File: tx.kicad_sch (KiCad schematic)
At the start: 44 parts, among them J5 SWH, J7 SMA, T2 RF_BALUN, U12 MAX2831, U13 TXIF_BALUN, U16 DPDT

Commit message: Add footprints
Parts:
- C86: footprint (none) -> Capacitor_SMD:C_0201_0603Metric
- FL2: footprint (none) -> mainboard:Filter_Pulse_LPF1005LL50R2400A_1.5x0.5mm
- J5: footprint (none) -> mainboard:Murata_SWH_MM8930-26xx
- J7: footprint (none) -> mainboard:Linx_SMA_CONSMA003.062
- L2, L6, L7: footprint (none) -> Inductor_SMD:L_0201_0603Metric
- T2: footprint (none) -> RF_Converter:Anaren_0805_2012Metric-6
- U13: footprint (none) -> mainboard:Balun_TDK_TFSZ06052460-3310A2X
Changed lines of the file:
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@@
       (effects (font (size 1.27 1.27)) (justify left))
     )
-    (property "Footprint" "" (at 111.76 80.01 0)
+    (property "Footprint" "Inductor_SMD:L_0201_0603Metric" (at 111.76 80.01 0)
       (effects (font (size 1.27 1.27)) hide)
     )
@@
       (effects (font (size 1.27 1.27)))
     )
-    (property "Footprint" "" (at 166.37 119.38 0)
+    (property "Footprint" "RF_Converter:Anaren_0805_2012Metric-6" (at 166.37 119.38 0)
       (effects (font (size 1.27 1.27)) hide)
     )
@@
       (effects (font (size 1.27 1.27)))
     )
-    (property "Footprint" "" (at 196.85 86.36 0)
+    (property "Footprint" "mainboard:Murata_SWH_MM8930-26xx" (at 196.85 86.36 0)
       (effects (font (size 1.27 1.27)) hide)
     )
@@
       (effects (font (size 1.27 1.27)) (justify left))
     )
-    (property "Footprint" "" (at 111.4552 148.59 0)
+    (property "Footprint" "Capacitor_SMD:C_0201_0603Metric" (at 111.4552 148.59 0)
       (effects (font (size 1.27 1.27)) hide)
     )
@@
       (effects (font (size 1.27 1.27)))
     )
-    (property "Footprint" "" (at 129.54 74.93 0)
+    (property "Footprint" "mainboard:Murata_SWH_MM8930-26xx" (at 129.54 74.93 0)
       (effects (font (size 1.27 1.27)) hide)
     )
@@
       (effects (font (size 1.27 1.27)) (justify left))
     )
-    (property "Footprint" "" (at 175.26 110.49 0)
+    (property "Footprint" "Inductor_SMD:L_0201_0603Metric" (at 175.26 110.49 0)
       (effects (font (size 1.27 1.27)) hide)
     )
@@
       (effects (font (size 1.27 1.27)) (justify left))
     )
-    (property "Footprint" "" (at 260.35 74.93 0)
+    (property "Footprint" "mainboard:Linx_SMA_CONSMA003.062" (at 260.35 74.93 0)
       (effects (font (size 1.27 1.27)) hide)
     )
@@
       (effects (font (size 1.27 1.27)))
     )
-    (property "Footprint" "" (at 146.05 62.23 0)
+    (property "Footprint" "mainboard:Filter_Pulse_LPF1005LL50R2400A_1.5x0.5mm" (at 146.05 62.23 0)
       (effects (font (size 1.27 1.27)) hide)
     )
@@
       (effects (font (size 1.27 1.27)))
     )
-    (property "Footprint" "" (at 242.57 120.65 0)
+    (property "Footprint" "mainboard:Balun_TDK_TFSZ06052460-3310A2X" (at 242.57 120.65 0)
       (effects (font (size 1.27 1.27)) hide)
     )
@@
     )
     (property "Part Number" "TFSZ06052460-3310A2X" (at 242.57 113.03 0)
+      (effects (font (size 1.27 1.27)) hide)
+    )
+    (property "Description" "BALUN 2300-2690 MHZ" (at 242.57 113.03 0)
       (effects (font (size 1.27 1.27)) hide)
     )
@@
       (effects (font (size 1.27 1.27)))
     )
-    (property "Footprint" "" (at 118.11 87.63 0)
+    (property "Footprint" "mainboard:Balun_TDK_TFSZ06052460-3310A2X" (at 118.11 87.63 0)
       (effects (font (size 1.27 1.27)) hide)
     )
@@
     )
     (property "Part Number" "TFSZ06052460-3310A2X" (at 118.11 80.01 0)
+      (effects (font (size 1.27 1.27)) hide)
+    )
+    (property "Description" "BALUN 2300-2690 MHZ" (at 118.11 80.01 0)
       (effects (font (size 1.27 1.27)) hide)
     )
@@
       (effects (font (size 1.27 1.27)) (justify left))
     )
-    (property "Footprint" "" (at 236.22 113.03 0)
-      (effects (font (size 1.27 1.27)) hide)
-    )
+    (property "Footprint" "Inductor_SMD:L_0201_0603Metric" (at 236.22 113.03 0)
+      (effects (font (size 1.27 1.27)) hide)
+    )

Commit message: Add more footprints
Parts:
- U16: footprint eval:QFN-12-1EP_2x2mm_P0.5mm_EP1x1mm -> mainboard:QFN-12-1EP_2x2mm_P0.5mm_EP1x1mm
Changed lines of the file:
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@@
       (effects (font (size 1.27 1.27)) (justify left))
     )
-    (property "Footprint" "eval:QFN-12-1EP_2x2mm_P0.5mm_EP1x1mm" (at 168.91 74.93 0)
+    (property "Footprint" "mainboard:QFN-12-1EP_2x2mm_P0.5mm_EP1x1mm" (at 168.91 74.93 0)
       (effects (font (size 1.27 1.27)) hide)
     )

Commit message: layout wip
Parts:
- added C10 (x2): 1uF, Capacitor_SMD:C_0201_0603Metric, symbol Device:C
- added J13: RFShield_Frame, RF_Shielding:Laird_Technologies_BMI-S-204-F_32.00x32.00mm, symbol Device:RFShield_OnePiece
- C36: footprint Capacitor_SMD:C_0402_1005Metric -> Capacitor_SMD:C_0201_0603Metric; Manufacturer Samsung -> Murata; Part Number CL05A105KP5NNNC -> GRM033R61A105ME44D; Substitution any equivalent -> GRM033R61A105ME44*, GRM033R61C105ME15*, Samsung CL03A105MO3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
- U16: footprint mainboard:QFN-12-1EP_2x2mm_P0.5mm_EP1x1mm -> mainboard:QFN-12-1EP_2x2mm_P0.5mm_EP1x1mm_ThermalVias
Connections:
- net 3V3TX: now also C10.1, C10.1
- net GND: now also C10.2, C10.2, J13.1 (Shield)
- net TX Mixer/MIX_IN+: now also L7.2, U13.4; no longer L7.1, U13.3
- net TX Mixer/MIX_IN-: now also L7.1, U13.3; no longer L7.2, U13.4

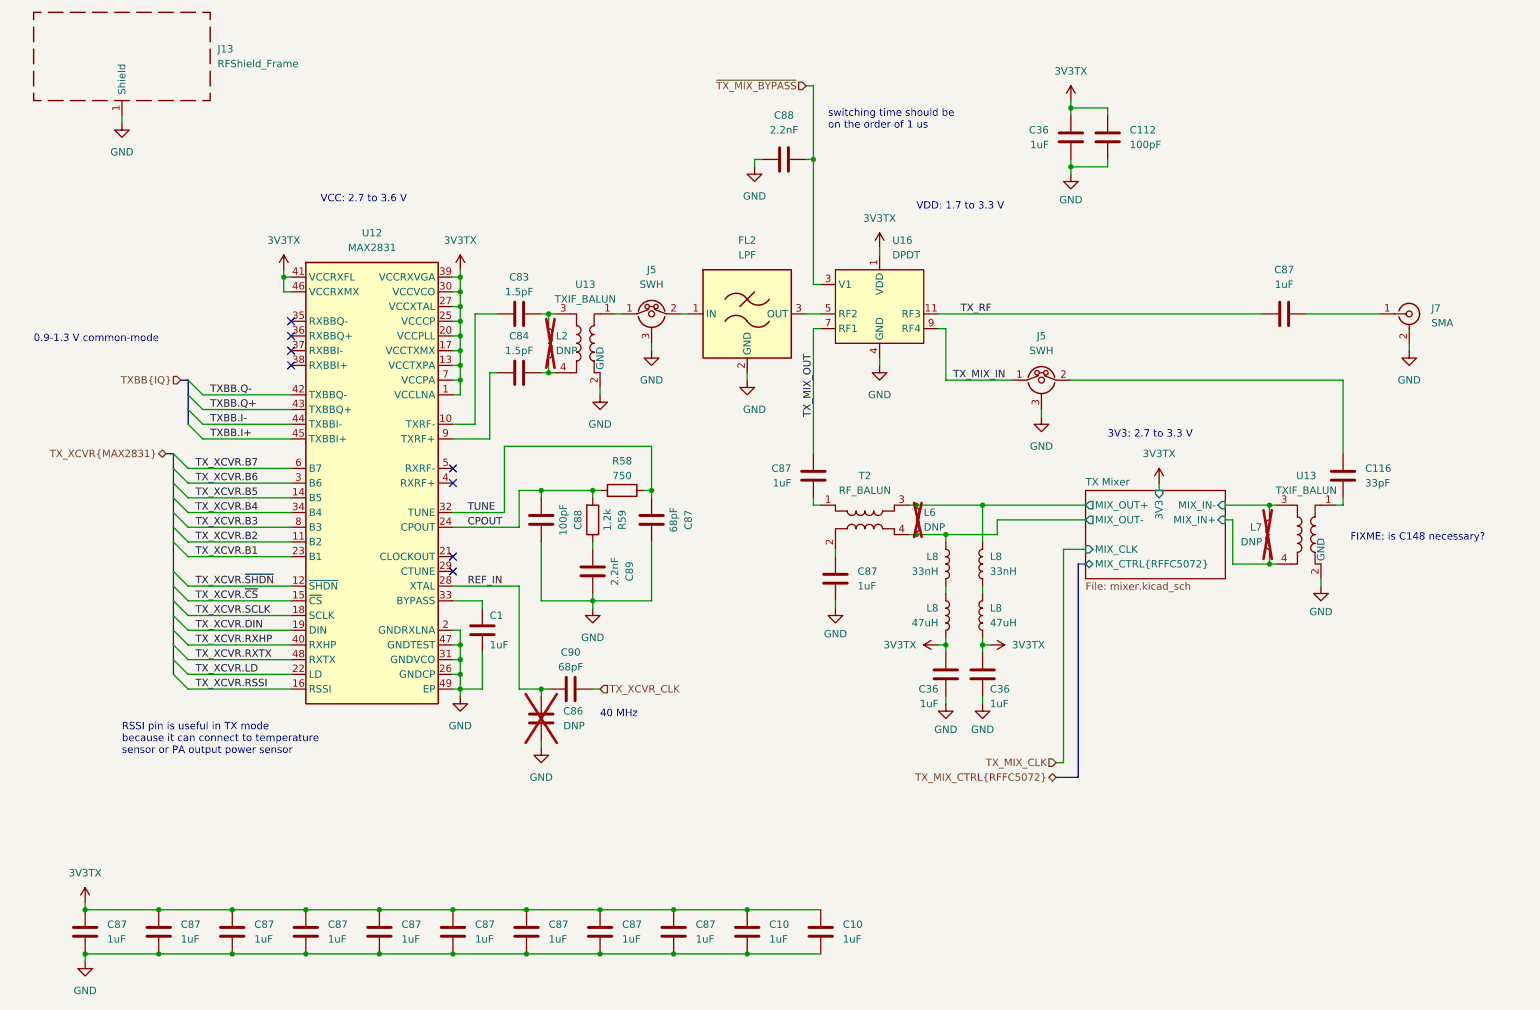
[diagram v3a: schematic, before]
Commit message: complete initial layout
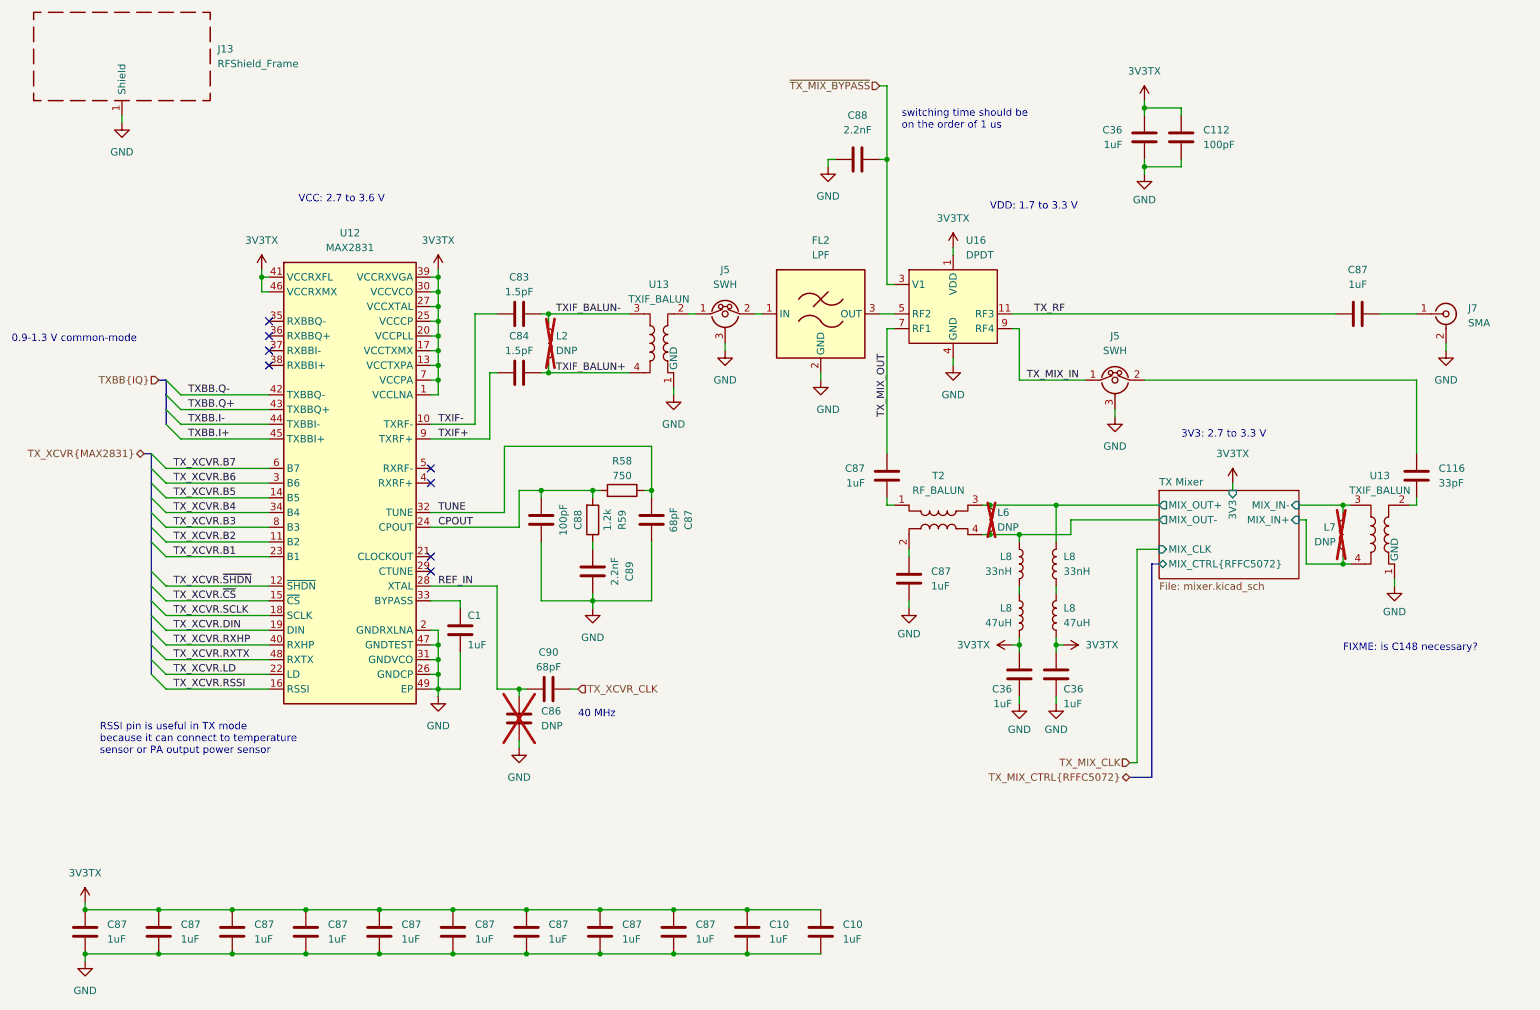
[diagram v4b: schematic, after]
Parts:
- U13: symbol Transformer:0896BM15A0001 -> radio:TFSZ06052460-3310A2X
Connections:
- net GND: now also U13.1 (GND), U13.1 (GND); no longer U13.2 (GND), U13.2 (GND), U13.5 (GND), U13.5 (GND), U13.6 (GND), U13.6 (GND)
- net TXIF_BALUN-: now reaches C83.2, L2.1, U13.3
- net TXIF_BALUN+: now reaches C84.2, L2.2, U13.4
- net TXIF-: now reaches C83.1, U12.10 (TXRF-)
- net at C116.2: now also U13.2; no longer U13.1
- net at J5.1 (C): now also U13.2; no longer U13.1
- net TXIF+: now reaches C84.1, U12.9 (TXRF+)
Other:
- moved on the sheet: C1, C112, C116, C36, C86, C87, C88, C90, FL2, J5, J7, L6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

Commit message: passive component selections
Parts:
- C83, C84: Manufacturer (none) -> Murata; Part Number (none) -> GRM0335C1H1R5CA01D; Substitution (none) -> GRM0335C1H1R5CA01*
- C87, C90: Manufacturer (none) -> Murata; Part Number (none) -> GRM0335C1H680JA01D; Substitution (none) -> GRM0335C1H680JA01*
- R58: Manufacturer (none) -> Yageo; Part Number (none) -> RC0201JR-07750RL; Substitution (none) -> any equivalent
- R59: Manufacturer (none) -> Yageo; Part Number (none) -> RC0201JR-071K2L; Substitution (none) -> any equivalent
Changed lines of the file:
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@@
+      (effects (font (size 1.27 1.27)) hide)
+    )
+    (property "Description" "RES 750 OHM 5% 1/20W 0201" (at 124.46 105.41 0)
+      (effects (font (size 1.27 1.27)) hide)
+    )
+    (property "Manufacturer" "Yageo" (at 124.46 105.41 0)
+      (effects (font (size 1.27 1.27)) hide)
+    )
+    (property "Part Number" "RC0201JR-07750RL" (at 124.46 105.41 0)
+      (effects (font (size 1.27 1.27)) hide)
+    )
+    (property "Substitution" "any equivalent" (at 124.46 105.41 0)
       (effects (font (size 1.27 1.27)) hide)
     )
@@
       (effects (font (size 1.27 1.27)) hide)
     )
+    (property "Description" "CAP CER 1.5PF 50V C0G/NP0 0201" (at 106.68 74.93 0)
+      (effects (font (size 1.27 1.27)) hide)
+    )
+    (property "Manufacturer" "Murata" (at 106.68 74.93 0)
+      (effects (font (size 1.27 1.27)) hide)
+    )
+    (property "Part Number" "GRM0335C1H1R5CA01D" (at 106.68 74.93 0)
+      (effects (font (size 1.27 1.27)) hide)
+    )
+    (property "Substitution" "GRM0335C1H1R5CA01*" (at 106.68 74.93 0)
+      (effects (font (size 1.27 1.27)) hide)
+    )
     (pin "1")
     (pin "2")
@@
       (effects (font (size 1.27 1.27)) hide)
     )
+    (property "Description" "CAP CER 68PF 50V C0G/NP0 0201" (at 111.76 139.7 0)
+      (effects (font (size 1.27 1.27)) hide)
+    )
+    (property "Manufacturer" "Murata" (at 111.76 139.7 0)
+      (effects (font (size 1.27 1.27)) hide)
+    )
+    (property "Part Number" "GRM0335C1H680JA01D" (at 111.76 139.7 0)
+      (effects (font (size 1.27 1.27)) hide)
+    )
+    (property "Substitution" "GRM0335C1H680JA01*" (at 111.76 139.7 0)
+      (effects (font (size 1.27 1.27)) hide)
+    )
     (pin "1")
     (pin "2")
@@
       (effects (font (size 1.27 1.27)) hide)
     )
+    (property "Description" "CAP CER 1.5PF 50V C0G/NP0 0201" (at 106.68 85.09 0)
+      (effects (font (size 1.27 1.27)) hide)
+    )
+    (property "Manufacturer" "Murata" (at 106.68 85.09 0)
+      (effects (font (size 1.27 1.27)) hide)
+    )
+    (property "Part Number" "GRM0335C1H1R5CA01D" (at 106.68 85.09 0)
+      (effects (font (size 1.27 1.27)) hide)
+    )
+    (property "Substitution" "GRM0335C1H1R5CA01*" (at 106.68 85.09 0)
+      (effects (font (size 1.27 1.27)) hide)
+    )
     (pin "1")
     (pin "2")
@@
     )
     (property "Datasheet" "~" (at 129.54 110.49 0)
+      (effects (font (size 1.27 1.27)) hide)
+    )
+    (property "Description" "CAP CER 68PF 50V C0G/NP0 0201" (at 129.54 110.49 0)
+      (effects (font (size 1.27 1.27)) hide)
+    )
+    (property "Manufacturer" "Murata" (at 129.54 110.49 0)
+      (effects (font (size 1.27 1.27)) hide)
+    )
+    (property "Part Number" "GRM0335C1H680JA01D" (at 129.54 110.49 0)
+      (effects (font (size 1.27 1.27)) hide)
+    )
+    (property "Substitution" "GRM0335C1H680JA01*" (at 129.54 110.49 0)
       (effects (font (size 1.27 1.27)) hide)
     )
@@
       (effects (font (size 1.27 1.27)) hide)
     )
+    (property "Description" "RES 1.2K OHM 5% 1/20W 0201" (at 119.38 110.49 0)
+      (effects (font (size 1.27 1.27)) hide)
+    )
+    (property "Manufacturer" "Yageo" (at 119.38 110.49 0)
+      (effects (font (size 1.27 1.27)) hide)
+    )
+    (property "Part Number" "RC0201JR-071K2L" (at 119.38 110.49 0)
+      (effects (font (size 1.27 1.27)) hide)
+    )
+    (property "Substitution" "any equivalent" (at 119.38 110.49 0)
+      (effects (font (size 1.27 1.27)) hide)
+    )
